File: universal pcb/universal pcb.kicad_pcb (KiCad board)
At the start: 2 copper layers, 30 x 22.5 mm, 6 parts

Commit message: KiCad Changes
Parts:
- turned LED to -40 degrees
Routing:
- net (no net): track 0.00 -> 260.0 mm
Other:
- board text added: "gnd"
- board text added: "led"
- board text added: "x"
- board text added: "y"
- board text added: "z"

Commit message: KiCad Changes
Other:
- board text added: "x1"
- board text added: "x2"
- board text added: "x3"
- board text added: "x4"
- board text added: "y1"
- board text added: "y2"
- board text added: "y3"
- board text added: "y4"
- board text added: "z1"
- board text added: "z2"
- board text added: "z3"
- board text added: "z4"
- board text removed: "1"
- board text removed: "10"
- board text removed: "11"
- board text removed: "12"
- board text removed: "2"
- board text removed: "3"
- board text removed: "4"
- board text removed: "5"
- board text removed: "6"
- board text removed: "7"
- board text removed: "8"
- board text removed: "9"
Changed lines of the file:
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@@
   (gr_line (start 15 0) (end 15 22.5) (layer "User.2") (width 0.1))
   (gr_line (start 0 11.25) (end 30 11.25) (layer "User.2") (width 0.1))
-  (gr_text "1" (at 27.2 7.25) (layer "B.SilkS")
-    (effects (font (size 0.8 0.8) (thickness 0.12)) (justify mirror))
+  (gr_text "z1" (at 27.75 9.548858) (layer "B.SilkS")
+    (effects (font (size 0.6 0.6) (thickness 0.1)) (justify left mirror))
   )
-  (gr_text "5" (at 27.2 13.65) (layer "B.SilkS")
-    (effects (font (size 0.8 0.8) (thickness 0.12)) (justify mirror))
+  (gr_text "gnd\n" (at 27.75 10.75) (layer "B.SilkS")
+    (effects (font (size 0.6 0.6) (thickness 0.1)) (justify left mirror))
   )
-  (gr_text "12" (at 3.15 15.25) (layer "B.SilkS")
-    (effects (font (size 0.8 0.8) (thickness 0.12)) (justify mirror))
+  (gr_text "x3" (at 27.75 12.016286) (layer "B.SilkS")
+    (effects (font (size 0.6 0.6) (thickness 0.1)) (justify left mirror))
   )
-  (gr_text "2" (at 27.2 8.85) (layer "B.SilkS")
-    (effects (font (size 0.8 0.8) (thickness 0.12)) (justify mirror))
+  (gr_text "gnd\n" (at 2.286 10.813142) (layer "B.SilkS")
+    (effects (font (size 0.6 0.6) (thickness 0.1)) (justify right mirror))
   )
-  (gr_text "10" (at 3.15 12.05) (layer "B.SilkS")
-    (effects (font (size 0.8 0.8) (thickness 0.12)) (justify mirror))
+  (gr_text "z4" (at 2.286 14.514284) (layer "B.SilkS")
+    (effects (font (size 0.6 0.6) (thickness 0.1)) (justify right mirror))
   )
-  (gr_text "7\n" (at 2.8 7.25) (layer "B.SilkS")
-    (effects (font (size 0.8 0.8) (thickness 0.12)) (justify mirror))
+  (gr_text "x4" (at 2.286 12.046856) (layer "B.SilkS")
+    (effects (font (size 0.6 0.6) (thickness 0.1)) (justify right mirror))
   )
-  (gr_text "11" (at 3.15 13.65) (layer "B.SilkS")
-    (effects (font (size 0.8 0.8) (thickness 0.12)) (justify mirror))
+  (gr_text "y3" (at 27.75 13.25) (layer "B.SilkS")
+    (effects (font (size 0.6 0.6) (thickness 0.1)) (justify left mirror))
   )
-  (gr_text "4" (at 27.2 12.05) (layer "B.SilkS")
-    (effects (font (size 0.8 0.8) (thickness 0.12)) (justify mirror))
+  (gr_text "x2" (at 2.286 7.112) (layer "B.SilkS")
+    (effects (font (size 0.6 0.6) (thickness 0.1)) (justify right mirror))
   )
-  (gr_text "6" (at 27.2 15.25) (layer "B.SilkS")
-    (effects (font (size 0.8 0.8) (thickness 0.12)) (justify mirror))
+  (gr_text "gnd" (at 27.75 15.71743) (layer "B.SilkS")
+    (effects (font (size 0.6 0.6) (thickness 0.1)) (justify left mirror))
   )
-  (gr_text "9" (at 2.8 10.45) (layer "B.SilkS")
-    (effects (font (size 0.8 0.8) (thickness 0.12)) (justify mirror))
+  (gr_text "y4" (at 2.286 13.28057) (layer "B.SilkS")
+    (effects (font (size 0.6 0.6) (thickness 0.1)) (justify right mirror))
   )
-  (gr_text "8" (at 2.8 8.85) (layer "B.SilkS")
-    (effects (font (size 0.8 0.8) (thickness 0.12)) (justify mirror))
+  (gr_text "y1" (at 27.75 8.315144) (layer "B.SilkS")
+    (effects (font (size 0.6 0.6) (thickness 0.1)) (justify left mirror))
   )
-  (gr_text "3" (at 27.2 10.45) (layer "B.SilkS")
-    (effects (font (size 0.8 0.8) (thickness 0.12)) (justify mirror))
+  (gr_text "z2" (at 2.286 9.579428) (layer "B.SilkS")
+    (effects (font (size 0.6 0.6) (thickness 0.1)) (justify right mirror))
+  )
+  (gr_text "y2" (at 2.286 8.345714) (layer "B.SilkS")
+    (effects (font (size 0.6 0.6) (thickness 0.1)) (justify right mirror))
+  )
+  (gr_text "x1" (at 27.75 7.08143) (layer "B.SilkS")
+    (effects (font (size 0.6 0.6) (thickness 0.1)) (justify left mirror))
+  )
+  (gr_text "z3" (at 27.75 14.483714) (layer "B.SilkS")
+    (effects (font (size 0.6 0.6) (thickness 0.1)) (justify left mirror))
+  )
+  (gr_text "led" (at 2.286 15.748) (layer "B.SilkS")
+    (effects (font (size 0.6 0.6) (thickness 0.1)) (justify right mirror))
   )
   (gr_text "y" (at -0.762 5.842) (layer "User.2")

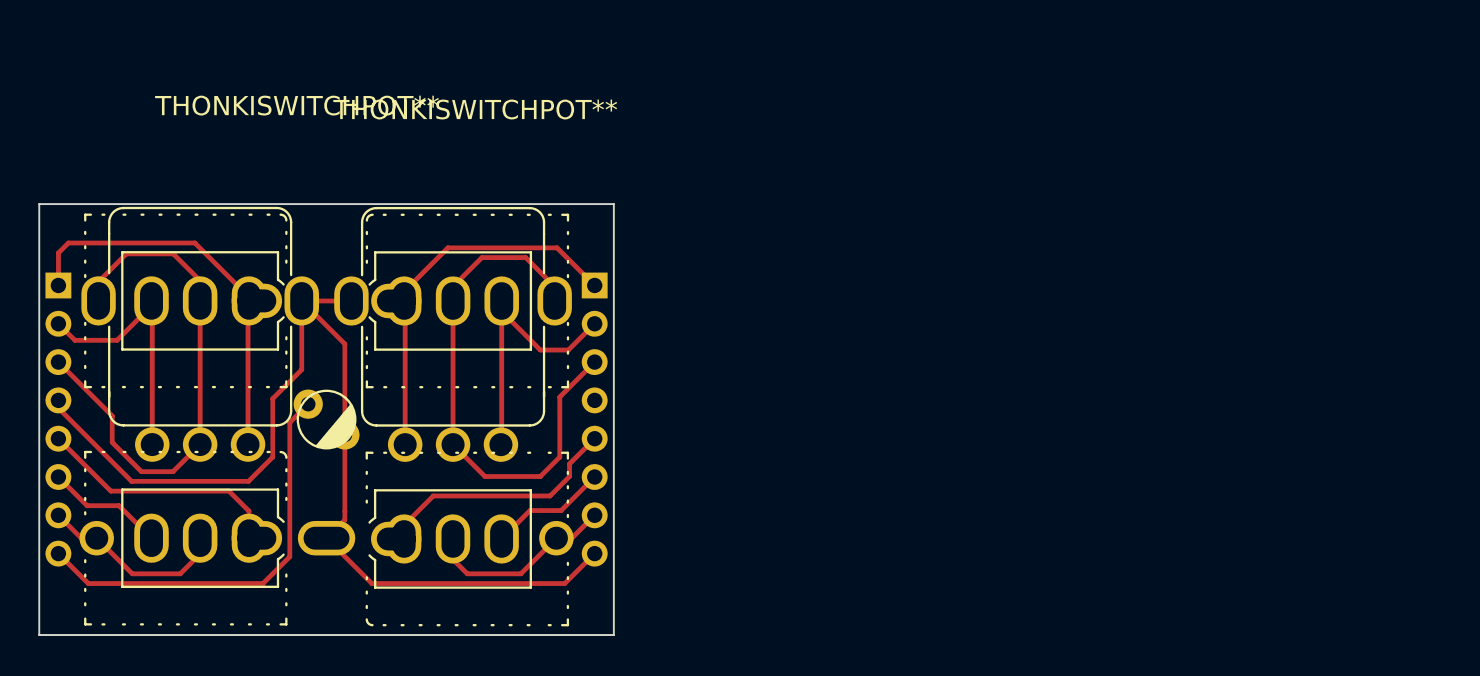
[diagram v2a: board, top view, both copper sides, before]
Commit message: KiCad Changes
Added backpack pcbs and backpack_template. Also changed headers to 2.54mm (still needs some cleanup)
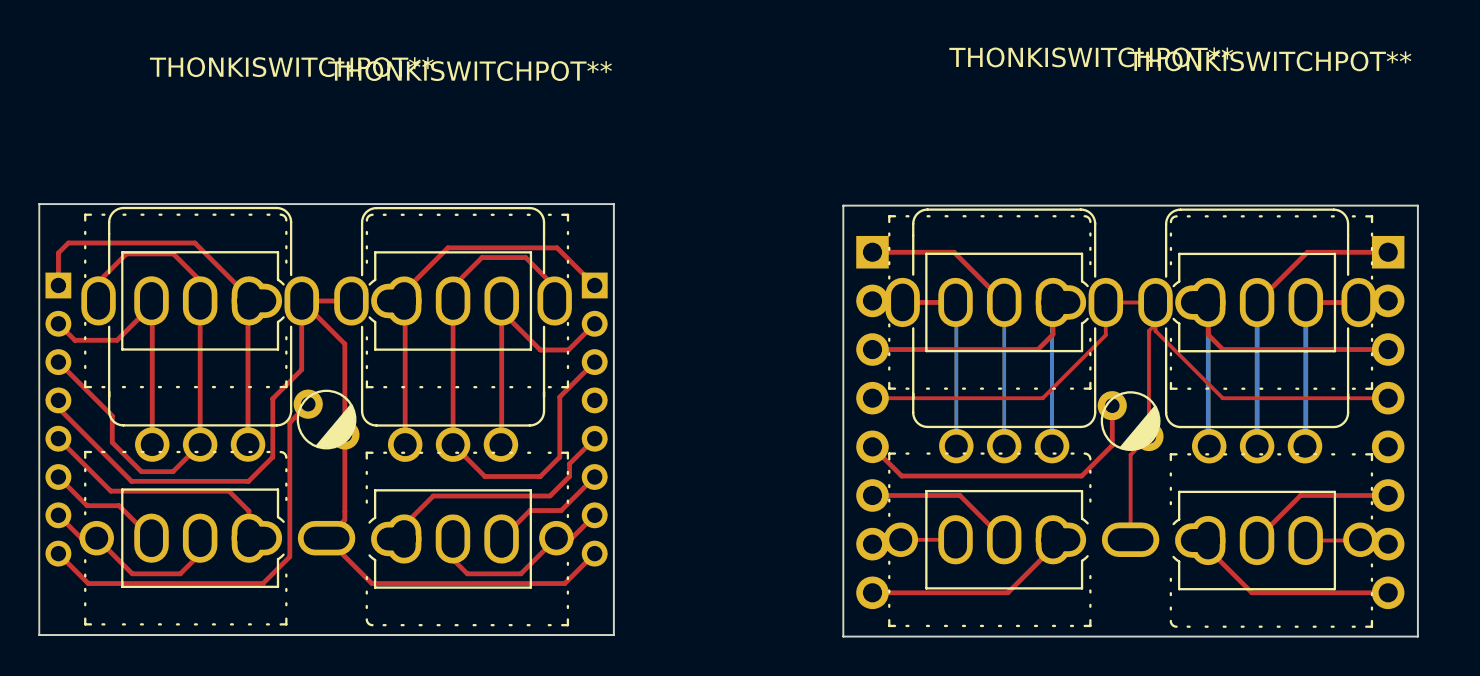
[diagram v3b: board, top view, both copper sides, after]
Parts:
- added LED: LED 3mm, Eurorack:LED 3mm, F.Cu at (57.0, 11.3)
- added REF**: PinHeader_1x08_P2.54mm_Vertical, Connector_PinHeader_2.54mm:PinHeader_1x08_P2.54mm_Vertical, B.Cu at (43.5, 2.52)
- added REF**: PinHeader_1x08_P2.54mm_Vertical, Connector_PinHeader_2.54mm:PinHeader_1x08_P2.54mm_Vertical, B.Cu at (70.4, 2.52)
- added THONK: Thonkiconn Dual, Eurorack:Thonkiconn Dual, F.Cu at (57.0, 17.5)
- added THONKISWITCHPOT**: Thonkiswitchpot Mirrored, Eurorack:Thonkiswitchpot Mirrored, F.Cu at (50.4, 5.14)
- added THONKISWITCHPOT**: Thonkiswitchpot, Eurorack:Thonkiswitchpot, F.Cu at (63.6, 5.14)
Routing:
- net (no net): track 260.0 -> 472.7 mm
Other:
- board size 30 x 22.5 mm -> 72 x 22.6 mm
- board text added: "2mm Version"
- board text added: "Alt 2.54mm Version WIP"

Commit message: KiCad Changes (2.54mm, cleaning up)
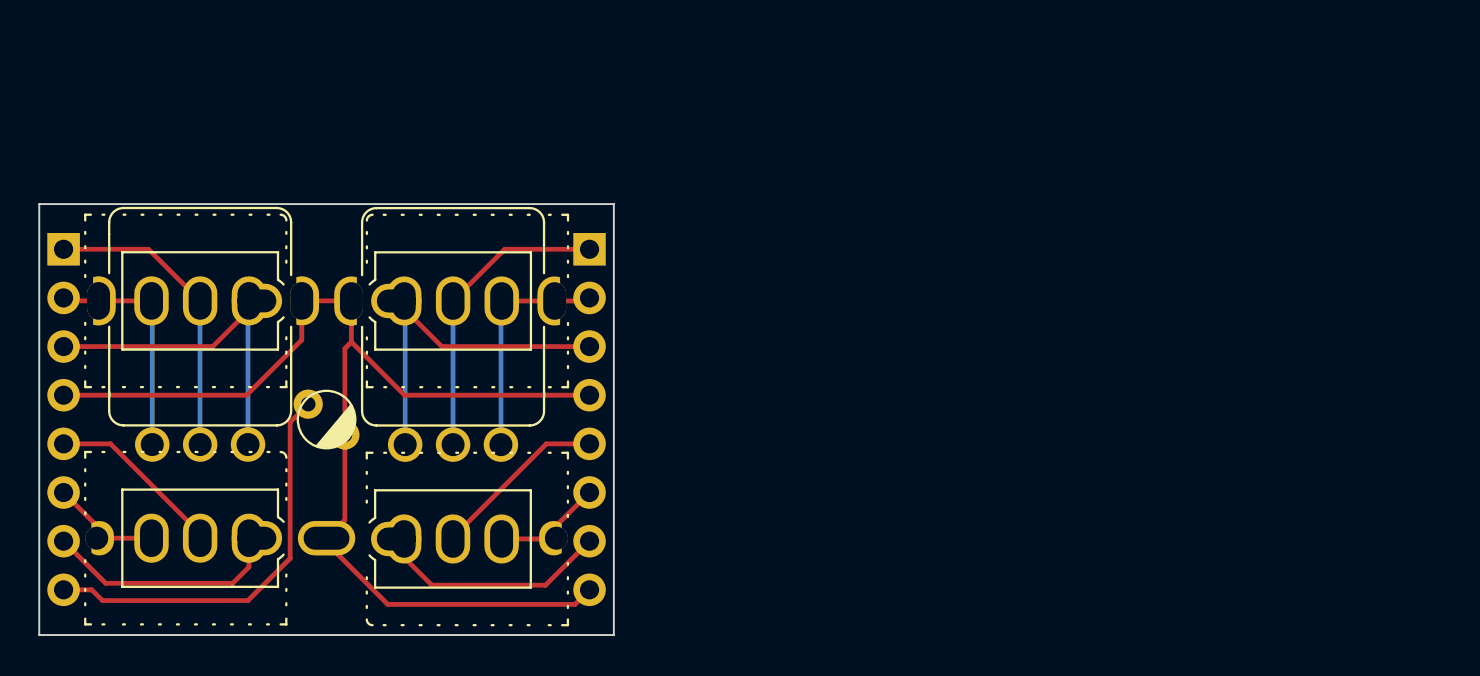
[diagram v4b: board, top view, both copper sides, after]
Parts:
- removed the LED at (15.0, 11.2)
- removed the REF** at (29.0, 4.25)
- removed the REF** at (1.00, 4.25)
- removed the THONK at (15.0, 17.4)
- removed the THONKISWITCHPOT** at (21.6, 5.06)
- removed the THONKISWITCHPOT** at (8.40, 5.05)
- moved REF** 42.2 mm to (1.27, 2.36)
- moved THONKISWITCHPOT** 42.0 mm to (8.40, 5.05)
- moved THONKISWITCHPOT** 42.0 mm to (21.6, 5.06)
- moved LED 42.0 mm to (15.0, 11.2)
- moved THONK 42.0 mm to (15.0, 17.4)
- moved REF** 41.7 mm to (28.7, 2.36)
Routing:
- net (no net): track 472.7 -> 231.5 mm
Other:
- board size 72 x 22.6 mm -> 30 x 22.5 mm
- board text removed: "2mm Version"
- board text removed: "Alt 2.54mm Version WIP"

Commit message: KiCad Changes
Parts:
- added REF**: LED_ASMB-KTF0-0A306, LED_SMD:LED_ASMB-KTF0-0A306, F.Cu at (15.0, 11.2)
- turned LED to 140 degrees
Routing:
- net (no net): track 231.5 -> 236.4 mm
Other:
- board text added: "blue"
- board text added: "green/led"
- board text added: "red"

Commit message: KiCad Changes
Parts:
- removed LED: LED 3mm, Eurorack:LED 3mm
- removed the REF** at (15.0, 11.2)
- added REF**: LED 3mm-SMD, Eurorack:LED 3mm-SMD, F.Cu at (15.0, 11.2)
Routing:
- net (no net): track 236.4 -> 235.1 mm
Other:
- board text removed: "led"

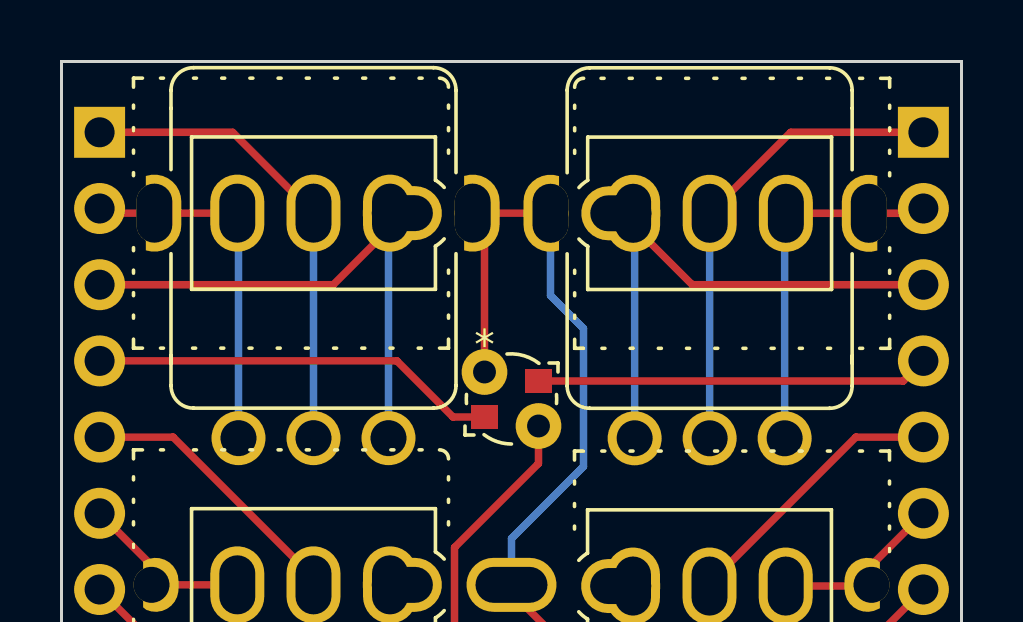
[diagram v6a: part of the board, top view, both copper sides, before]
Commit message: Add tactile switch footprints
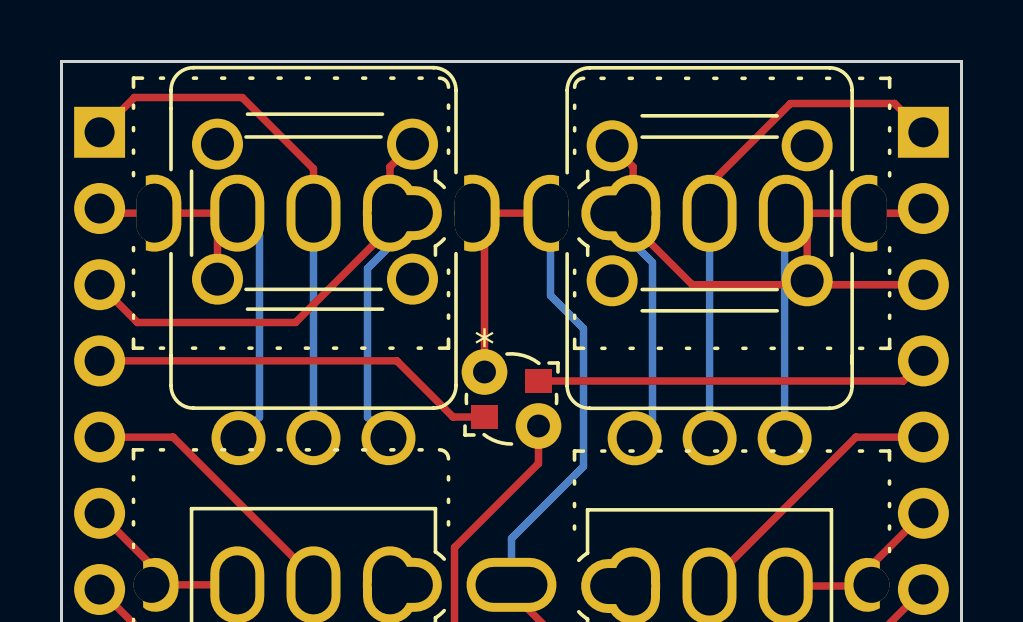
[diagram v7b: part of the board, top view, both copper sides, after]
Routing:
- net (no net): track 235.1 -> 251.2 mm

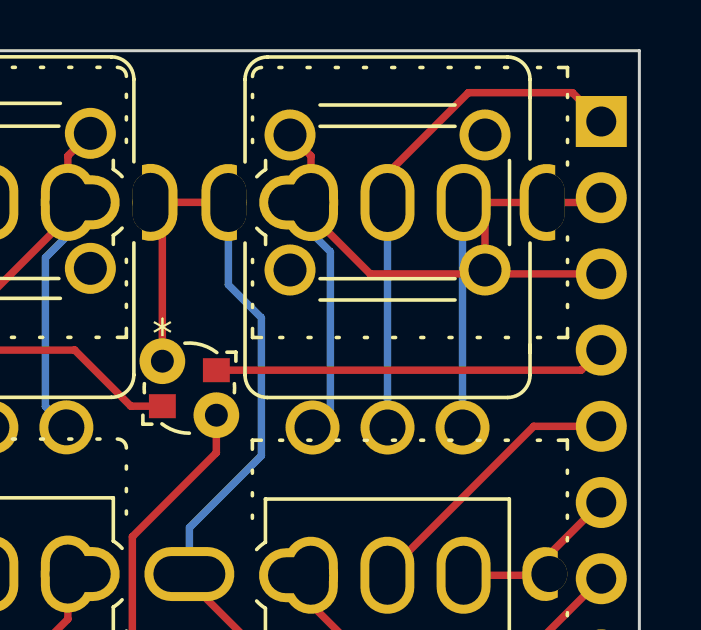
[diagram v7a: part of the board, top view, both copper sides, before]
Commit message: Create passive attenuator
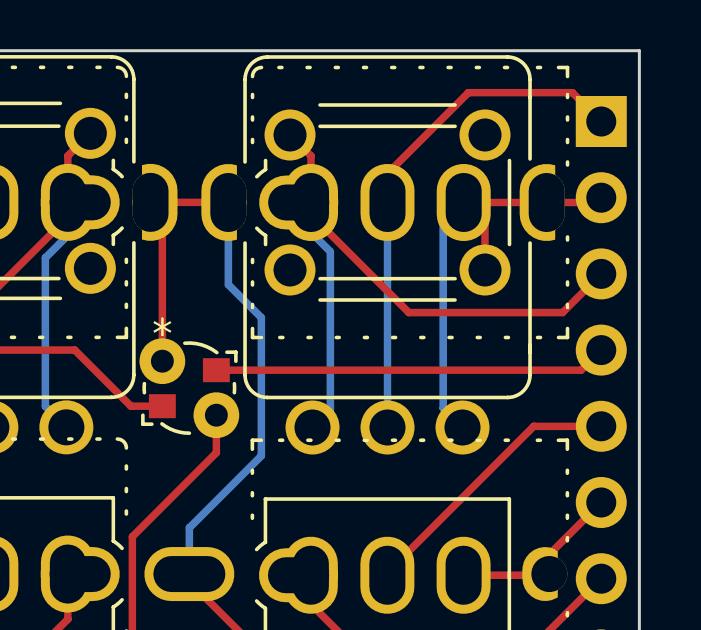
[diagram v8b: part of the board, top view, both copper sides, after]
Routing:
- net (no net): track 251.2 -> 252.8 mm
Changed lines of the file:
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@@
   (segment (start 3.095 5.055) (end 1.425 5.055) (width 0.25) (layer "F.Cu") (net 0))
   (segment (start 27.97 20.9) (end 18.2 20.9) (width 0.25) (layer "F.Cu") (net 0))
-  (segment (start 18.645 5.06) (end 21.025 7.44) (width 0.25) (layer "F.Cu") (net 0))
   (segment (start 3 17.445) (end 3 16.79) (width 0.25) (layer "F.Cu") (net 0))
   (segment (start 12.2 20.7) (end 1.83 20.7) (width 0.25) (layer "F.Cu") (net 0))
@@
   (segment (start 1.83 20.7) (end 1.27 20.14) (width 0.25) (layer "F.Cu") (net 0))
   (segment (start 26.96 17.485) (end 27 17.445) (width 0.25) (layer "F.Cu") (net 0))
+  (segment (start 18.645 5.06) (end 22.315 8.73) (width 0.25) (layer "F.Cu") (net 0))
   (segment (start 3 16.79) (end 1.27 15.06) (width 0.25) (layer "F.Cu") (net 0))
   (segment (start 3.72 12.52) (end 1.27 12.52) (width 0.25) (layer "F.Cu") (net 0))
@@
   (segment (start 26.43 19.9) (end 28.73 17.6) (width 0.25) (layer "F.Cu") (net 0))
   (segment (start 24.855 7.31) (end 24.855 5.77) (width 0.25) (layer "F.Cu") (net 0))
+  (segment (start 22.315 8.73) (end 27.44 8.73) (width 0.25) (layer "F.Cu") (net 0))
   (segment (start 10.95 3.505) (end 11.7 2.755) (width 0.25) (layer "F.Cu") (net 0))
   (segment (start 21.605 4.095) (end 21.605 5.06) (width 0.25) (layer "F.Cu") (net 0))
@@
   (segment (start 8.4 17.2) (end 3.72 12.52) (width 0.25) (layer "F.Cu") (net 0))
   (segment (start 21.6 17.485) (end 21.6 17.4) (width 0.25) (layer "F.Cu") (net 0))
-  (segment (start 21.025 7.44) (end 28.73 7.44) (width 0.25) (layer "F.Cu") (net 0))
   (segment (start 19.055 5.06) (end 19.055 3.51) (width 0.25) (layer "F.Cu") (net 0))
   (segment (start 15.9 13.4) (end 13.1 16.2) (width 0.25) (layer "F.Cu") (net 0))
@@
   (segment (start 1.27 2.36) (end 2.43 1.2) (width 0.25) (layer "F.Cu") (net 0))
   (segment (start 5.2 5.715) (end 5.86 5.055) (width 0.25) (layer "F.Cu") (net 0))
+  (segment (start 27.44 8.73) (end 28.73 7.44) (width 0.25) (layer "F.Cu") (net 0))
   (segment (start 1.27 17.6) (end 3.47 19.8) (width 0.25) (layer "F.Cu") (net 0))
   (segment (start 28.73 2.36) (end 27.77 1.4) (width 0.25) (layer "F.Cu") (net 0))
@@
   (segment (start 16.3 7.8) (end 16.3 5.06) (width 0.25) (layer "B.Cu") (net 0))
   (segment (start 15 17.445) (end 15 15.9) (width 0.25) (layer "B.Cu") (net 0))
+  (segment (start 24.105 12.56) (end 23.46 11.915) (width 0.25) (layer "B.Cu") (net 0))
+  (segment (start 23.46 5.745) (end 24.145 5.06) (width 0.25) (layer "B.Cu") (net 0))
   (segment (start 15 15.9) (end 17.4 13.5) (width 0.25) (layer "B.Cu") (net 0))
   (segment (start 19.055 6.055) (end 19.055 5.06) (width 0.25) (layer "B.Cu") (net 0))
@@
   (segment (start 17.4 8.9) (end 16.3 7.8) (width 0.25) (layer "B.Cu") (net 0))
   (segment (start 19.7 6.7) (end 19.055 6.055) (width 0.25) (layer "B.Cu") (net 0))
-  (segment (start 24.105 5.1) (end 24.145 5.06) (width 0.25) (layer "B.Cu") (net 0))
   (segment (start 17.4 13.5) (end 17.4 8.9) (width 0.25) (layer "B.Cu") (net 0))
   (segment (start 6.6 5.795) (end 5.86 5.055) (width 0.25) (layer "B.Cu") (net 0))
-  (segment (start 24.105 12.56) (end 24.105 5.1) (width 0.25) (layer "B.Cu") (net 0))
   (segment (start 21.605 12.56) (end 21.605 5.06) (width 0.25) (layer "B.Cu") (net 0))
   (segment (start 10.2 6.9) (end 10.95 6.15) (width 0.25) (layer "B.Cu") (net 0))
@@
   (segment (start 10.2 11.855) (end 10.2 6.9) (width 0.25) (layer "B.Cu") (net 0))
   (segment (start 5.9 12.555) (end 6.6 11.855) (width 0.25) (layer "B.Cu") (net 0))
+  (segment (start 23.46 11.915) (end 23.46 5.745) (width 0.25) (layer "B.Cu") (net 0))
   (segment (start 6.6 11.855) (end 6.6 5.795) (width 0.25) (layer "B.Cu") (net 0))
 )
